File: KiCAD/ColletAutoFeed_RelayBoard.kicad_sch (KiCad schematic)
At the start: 2 parts, among them J1 1761685-6, U1 ProS3

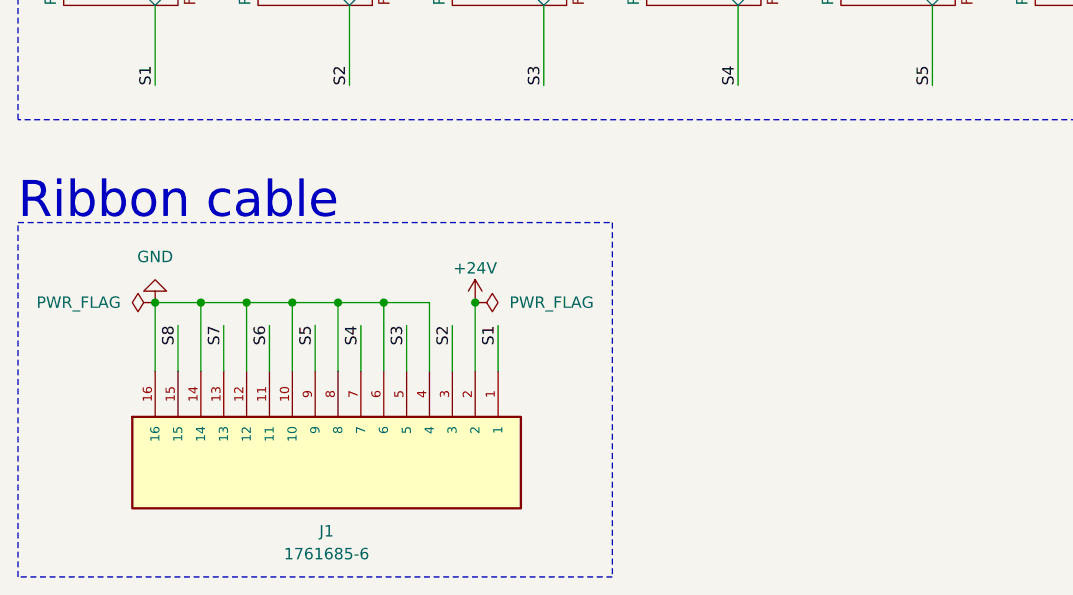
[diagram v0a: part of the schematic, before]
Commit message: Replaced ribbon cable connector with 10-pin molex
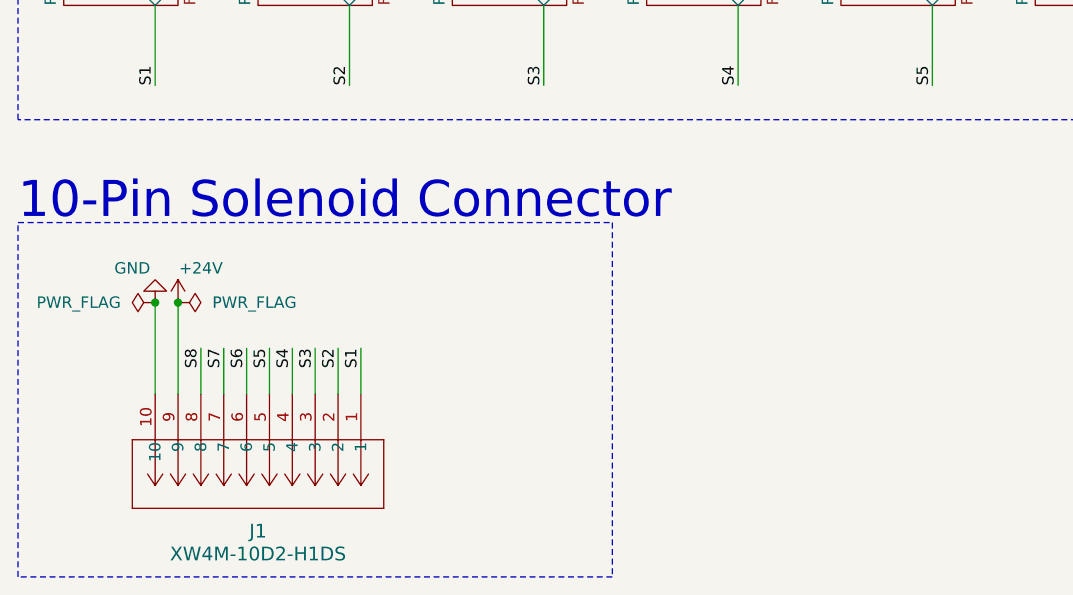
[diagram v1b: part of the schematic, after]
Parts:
- removed J1: 1761685-6, Vertical Header - Locking:TE_1761685-6, symbol Vertical Header - Locking:1761685-6
- added J1: XW4M-10D2-H1DS, xw4m-10d2-h1ds:xw4m-10d2-h1ds, symbol xw4m-10d2-h1ds:XW4M-10D2-H1DS
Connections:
- net +24V: now also J1.9
- net GND: now also J1.10
- net S1: now also J1.1
- net S2: now also J1.2
- net S3: now also J1.3
- net S4: now also J1.4
- net S5: now also J1.5
- net S6: now also J1.6
- net S7: now also J1.7
- net S8: now also J1.8
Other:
- note added: "10-Pin Solenoid Connector"
- note removed: "Ribbon cable"

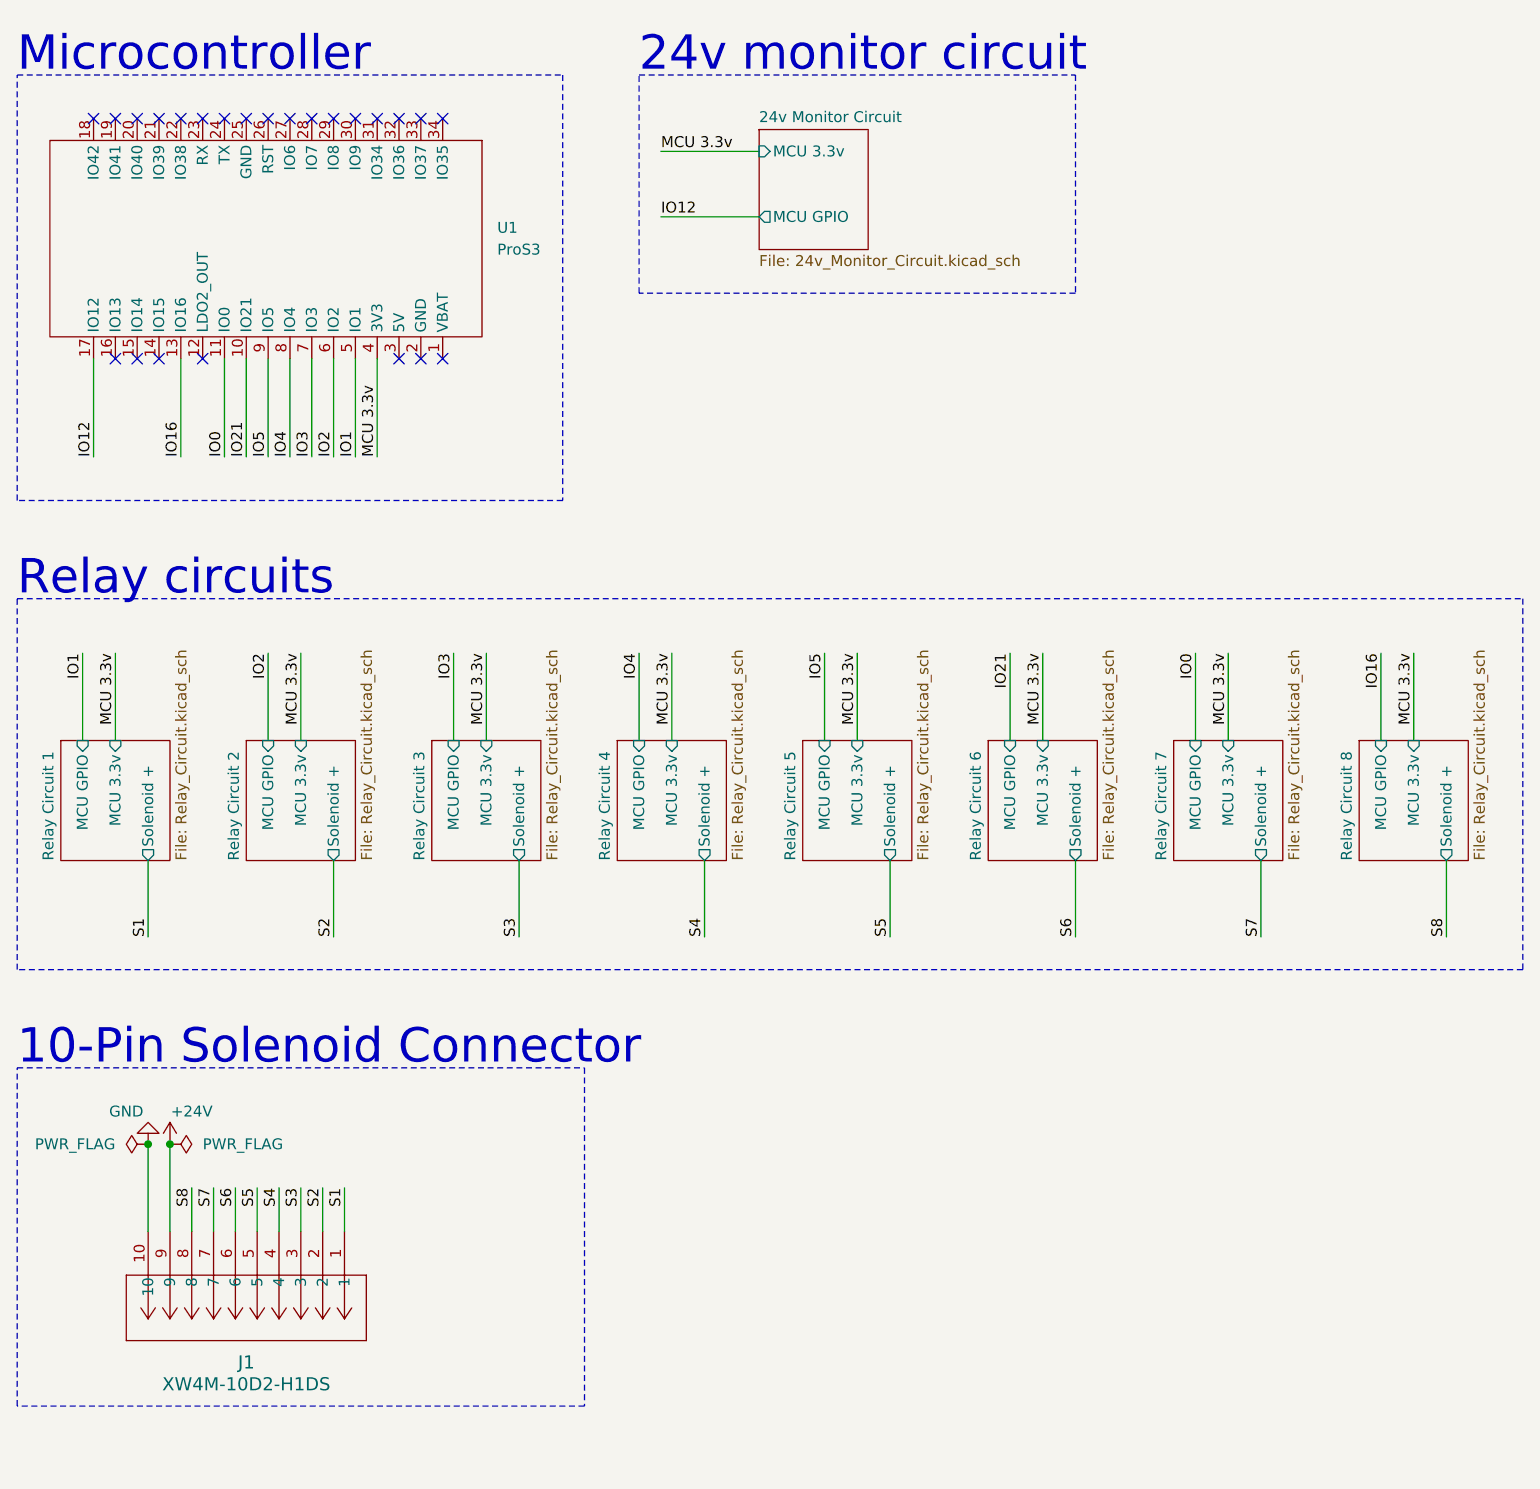
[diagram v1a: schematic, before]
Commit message: Updated board to new size
Updated board outline, stripped all old routing, added 2 pin omron power connector
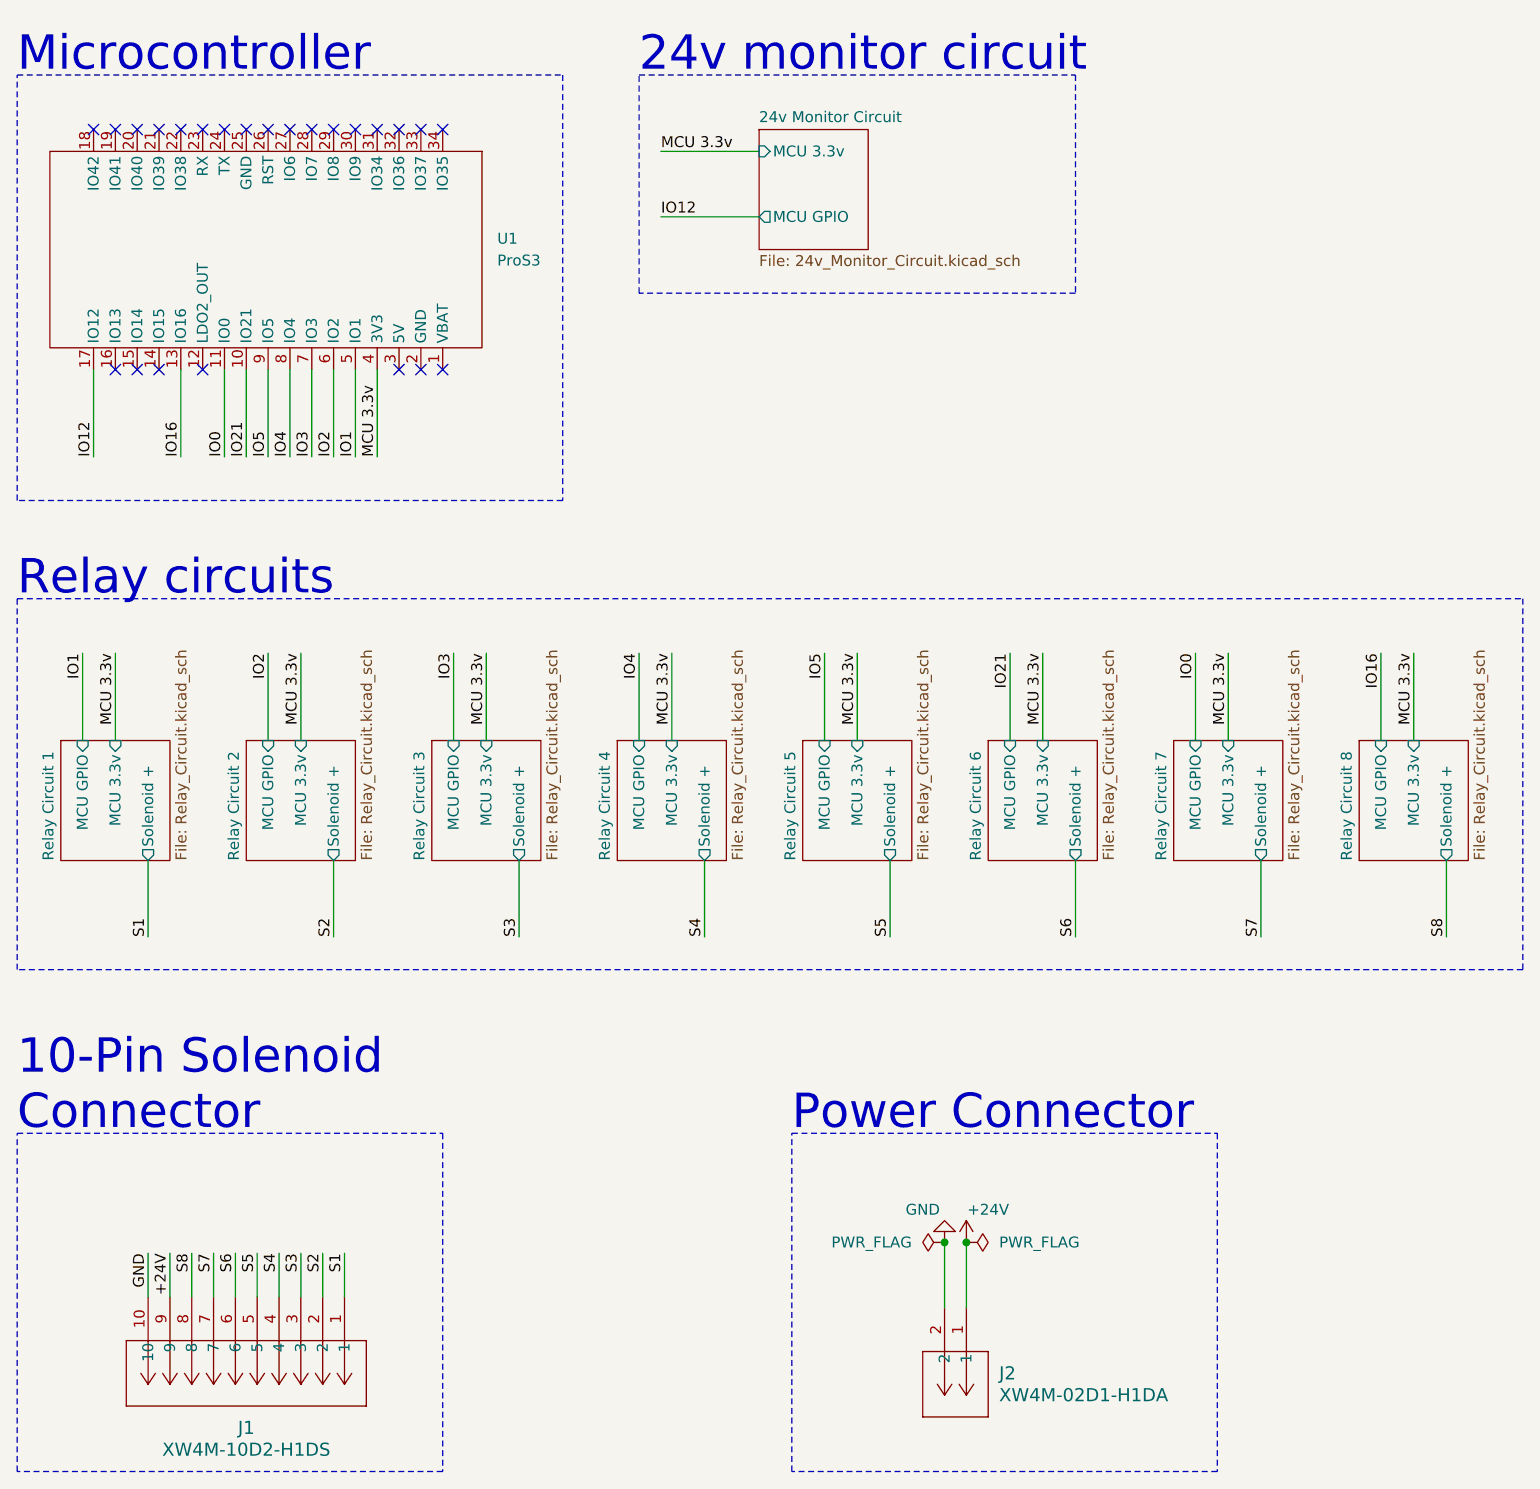
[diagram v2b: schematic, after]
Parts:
- added J2: XW4M-02D1-H1DA, xw4m-02d1-h1da, symbol xw4m-02d1-h1da:XW4M-02D1-H1DA
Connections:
- net +24V: now also J2.1
- net GND: now also J2.2
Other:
- note added: "Power Connector"
- moved on the sheet: J1, U1

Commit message: Placed components and routed traces on PCB
Placed components and completed initial routing. Still need to add power and ground planes and figure out silkscreen.
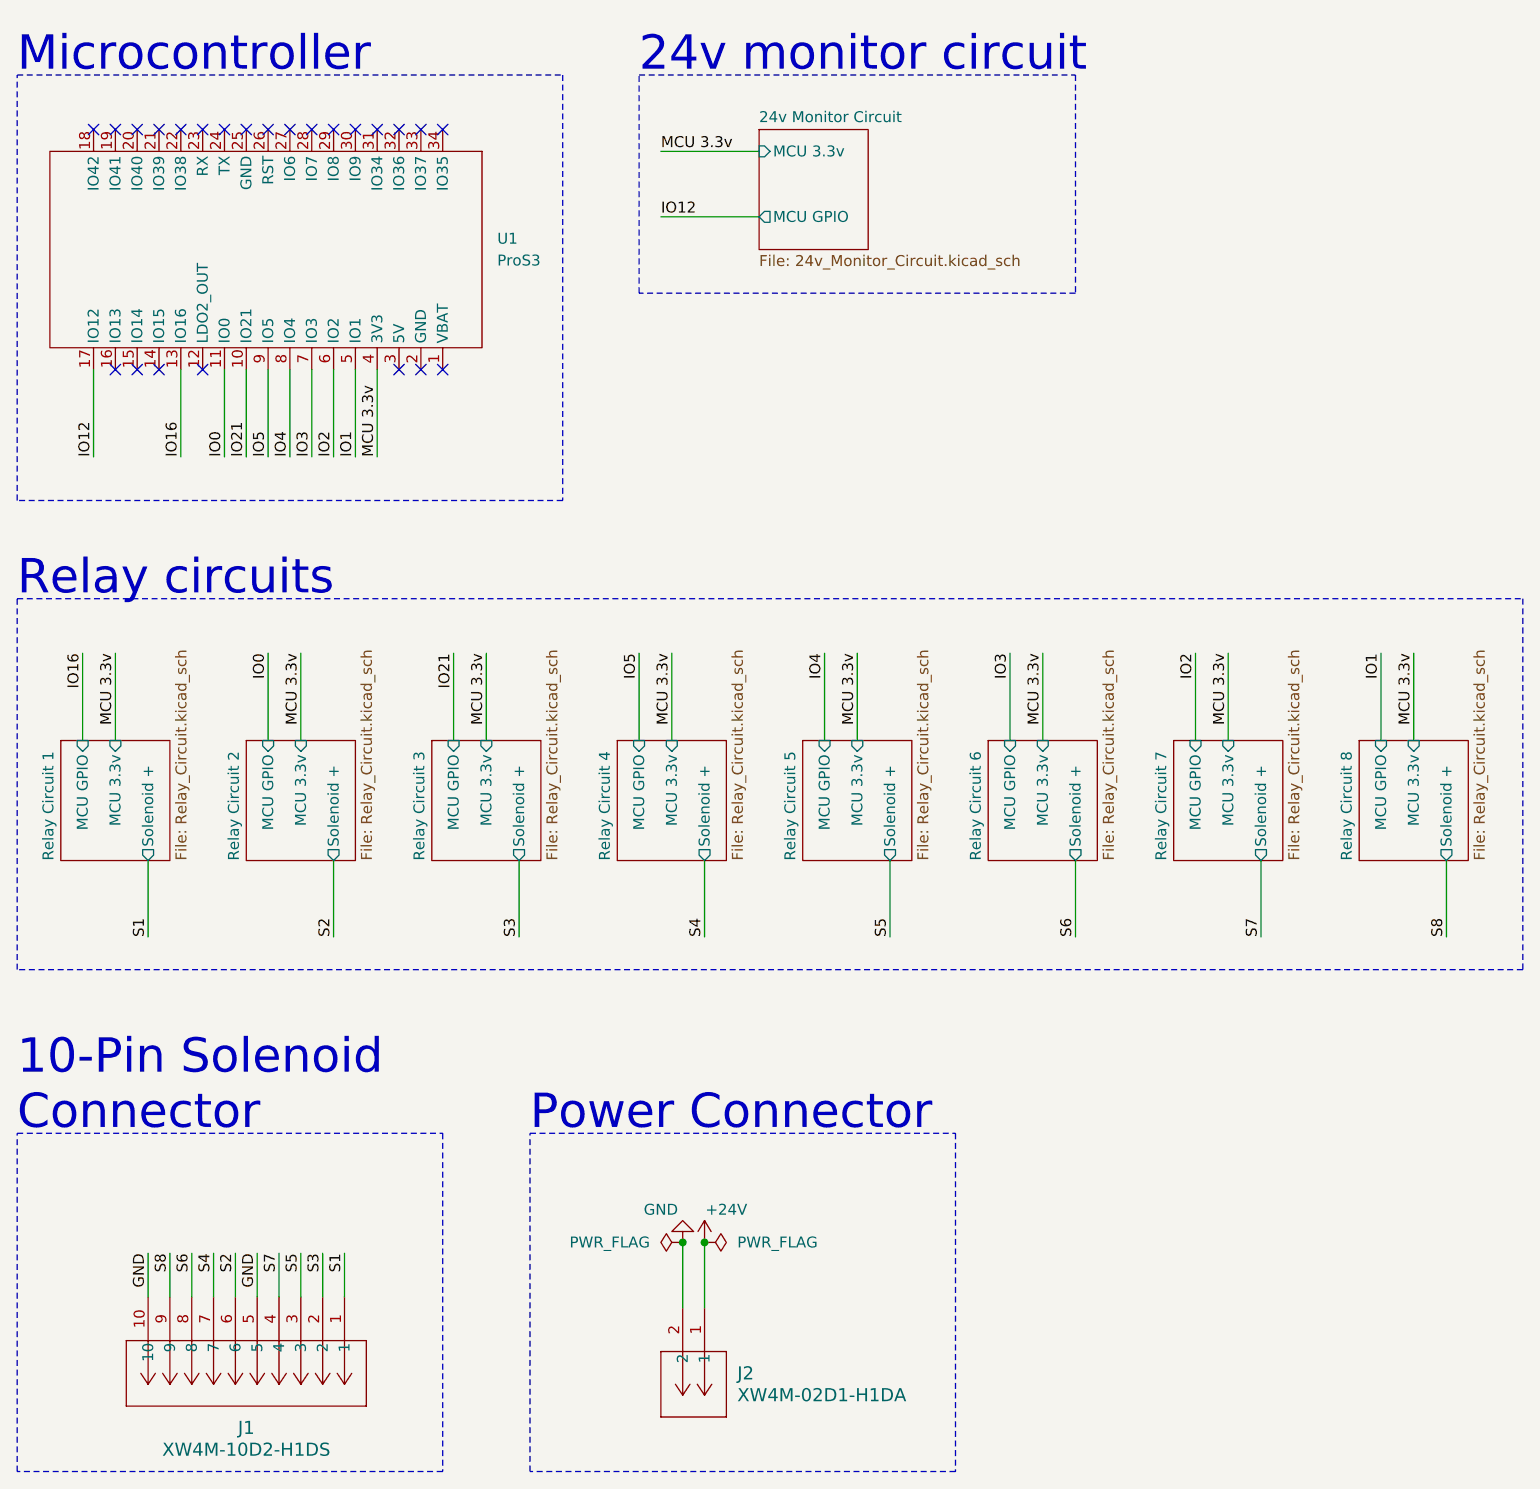
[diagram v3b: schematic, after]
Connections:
- net +24V: no longer J1.9
- net GND: now also J1.5
- net S2: now also J1.6; no longer J1.2
- net S3: now also J1.2; no longer J1.3
- net S4: now also J1.7; no longer J1.4
- net S5: now also J1.3; no longer J1.5
- net S6: now also J1.8; no longer J1.6
- net S7: now also J1.4; no longer J1.7
- net S8: now also J1.9; no longer J1.8
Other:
- moved on the sheet: J2

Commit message: Fixed Silkscreen Labels for Components
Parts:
- J2: footprint xw4m-02d1-h1da -> xw4m-02d1-h1da:xw4m-02d1-h1da
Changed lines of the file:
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@@
       (effects (font (size 1.524 1.524)) (justify left))
     )
-    (property "Footprint" "xw4m-02d1-h1da" (at 107.95 167.64 0)
+    (property "Footprint" "xw4m-02d1-h1da:xw4m-02d1-h1da" (at 107.95 167.64 0)
       (effects (font (size 1.27 1.27) italic) hide)
     )
